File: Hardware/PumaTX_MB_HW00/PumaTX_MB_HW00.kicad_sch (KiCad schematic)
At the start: 107 parts, among them J100 FH12A-26S-0.5SH_55_, J101 FH12-12S-0.5SH_55_, J102 500334-0160, J103 500334-0160, J104 692122030100, J105 53398-0667, J300 U.FL-R-SMT-1_40_, J410 U.FL-R-SMT-1_40_, M130 Motor_DC, M140 Fan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

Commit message: quick esp32 update
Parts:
- U300, U400: footprint Component_lib:ESP32-PICO-D4_1 -> ESP32-PICO-D4_1
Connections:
- net SYS is gone; now on net VSYS: R506.1, R507.1
- net GND: now also U300.49 (GND), U400.49 (GND)
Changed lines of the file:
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@@
     (effects (font (size 1.27 1.27)) (justify right bottom))
   )
-  (label "SYS" (at 449.58 269.24 0)
+  (label "VSYS" (at 449.58 269.24 0)
     (effects (font (size 1.27 1.27)) (justify left bottom))
   )
@@
     (pin "1")
   )
-  (symbol (lib_name "ESP32-PICO-D4_1") (lib_id "Component_lib:ESP32-PICO-D4") (at 73.66 231.14 0) (unit 1)
+  (symbol (lib_id "Component_lib:ESP32-PICO-D4") (at 73.66 231.14 0) (unit 1)
     (in_bom yes) (on_board yes)
     (property "Reference" "U300" (id 0) (at 76.2 223.52 0))
     (property "Value" "ESP32-PICO-D4" (id 1) (at 96.52 248.92 0))
-    (property "Footprint" "Component_lib:ESP32-PICO-D4_1" (id 2) (at 128.27 197.485 0)
+    (property "Footprint" "ESP32-PICO-D4_1" (id 2) (at 128.27 197.485 0)
       (effects (font (size 1.27 1.27)) (justify left) hide)
     )
@@
     (pin "47")
     (pin "48")
+    (pin "49")
     (pin "5")
     (pin "6")
@@
     (pin "2")
   )
-  (symbol (lib_name "ESP32-PICO-D4_1") (lib_id "Component_lib:ESP32-PICO-D4") (at 226.06 231.14 0) (unit 1)
+  (symbol (lib_id "Component_lib:ESP32-PICO-D4") (at 226.06 231.14 0) (unit 1)
     (in_bom yes) (on_board yes)
     (property "Reference" "U400" (id 0) (at 226.06 223.52 0))
     (property "Value" "ESP32-PICO-D4" (id 1) (at 248.92 248.92 0))
-    (property "Footprint" "Component_lib:ESP32-PICO-D4_1" (id 2) (at 280.67 197.485 0)
+    (property "Footprint" "ESP32-PICO-D4_1" (id 2) (at 280.67 197.485 0)
       (effects (font (size 1.27 1.27)) (justify left) hide)
     )
@@
     (pin "47")
     (pin "48")
+    (pin "49")
     (pin "5")
     (pin "6")
@@
     (pin "1")
   )
+  (symbol (lib_id "power:GND") (at 254 248.92 0) (unit 1)
+    (in_bom yes) (on_board yes) (fields_autoplaced)
+    (property "Reference" "#PWR0208" (id 0) (at 254 255.27 0)
+      (effects (font (size 1.27 1.27)) hide)
+    )
+    (property "Value" "GND" (id 1) (at 254 253.3634 0))
+    (property "Footprint" "" (id 2) (at 254 248.92 0)
+      (effects (font (size 1.27 1.27)) hide)
+    )
+    (property "Datasheet" "" (id 3) (at 254 248.92 0)
+      (effects (font (size 1.27 1.27)) hide)
+    )
+    (pin "1")
+  )
   (symbol (lib_id "power:GND") (at 101.6 167.64 0) (mirror y) (unit 1)
     (in_bom yes) (on_board yes) (fields_autoplaced)
@@
     (pin "1")
   )
+  (symbol (lib_id "power:GND") (at 101.6 248.92 0) (unit 1)
+    (in_bom yes) (on_board yes) (fields_autoplaced)
+    (property "Reference" "#PWR0209" (id 0) (at 101.6 255.27 0)
+      (effects (font (size 1.27 1.27)) hide)
+    )
+    (property "Value" "GND" (id 1) (at 101.6 253.3634 0))
+    (property "Footprint" "" (id 2) (at 101.6 248.92 0)
+      (effects (font (size 1.27 1.27)) hide)
+    )
+    (property "Datasheet" "" (id 3) (at 101.6 248.92 0)
+      (effects (font (size 1.27 1.27)) hide)
+    )
+    (pin "1")
+  )
   (symbol (lib_id "Component_lib:R") (at 439.42 246.38 0) (unit 1)
     (in_bom yes) (on_board yes) (fields_autoplaced)
@@
       (reference "#PWR0207") (unit 1) (value "GND") (footprint "")
     )
+    (path "/8a8d2f55-b2eb-4606-93f7-9e68a6db2d19"
+      (reference "#PWR0208") (unit 1) (value "GND") (footprint "")
+    )
+    (path "/a3bb5541-60f1-4243-b6fd-f9f2eee4e164"
+      (reference "#PWR0209") (unit 1) (value "GND") (footprint "")
+    )
     (path "/aa4b37d0-de21-49e4-a60d-a36a4900ab77"
       (reference "#VBAT0101") (unit 1) (value "VBAT") (footprint "")
@@
     )
     (path "/7c01edc0-d7f2-45db-8ab5-251f557b0984"
-      (reference "U300") (unit 1) (value "ESP32-PICO-D4") (footprint "Component_lib:ESP32-PICO-D4_1")
+      (reference "U300") (unit 1) (value "ESP32-PICO-D4") (footprint "ESP32-PICO-D4_1")
     )
     (path "/832e275b-682a-4d6c-91a4-f7dc151a03b6"
-      (reference "U400") (unit 1) (value "ESP32-PICO-D4") (footprint "Component_lib:ESP32-PICO-D4_1")
+      (reference "U400") (unit 1) (value "ESP32-PICO-D4") (footprint "ESP32-PICO-D4_1")
     )
     (path "/6f8f7369-26dc-458b-8b40-9bd8047cb234"

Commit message: working on routing / placement
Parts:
- removed ANT400: 2450AT18A100E, Component_lib:ANTC3216X140N, symbol Component_lib:2450AT18A100E
- removed J300: U.FL-R-SMT-1_40_, Component_lib:u.fl, symbol Component_lib:U.FL-R-SMT-1_40_
- added ANT300: 2450AT18A100E, Component_lib:ANTC3216X140N, symbol Component_lib:2450AT18A100E
- added C130, C140: 100n, Capacitor_SMD:C_0402_1005Metric, symbol Component lib:C
- added J400: U.FL-R-SMT-1_40_, Component_lib:u.fl, symbol Component_lib:U.FL-R-SMT-1_40_
- added R305: 120k, Capacitor_SMD:C_0402_1005Metric, symbol Component lib:R
- added R306: 470k, Capacitor_SMD:C_0402_1005Metric, symbol Component lib:R
- added R511, R512: 0, Capacitor_SMD:C_0201_0603Metric, symbol Component lib:R
- added TP105: BAT_WHITE, TestPoint:TestPoint_Pad_D1.0mm, symbol Connector:TestPoint
- added TP302: CRSF, TestPoint:TestPoint_Pad_D1.0mm, symbol Connector:TestPoint
- TP300, TP301, TP401: footprint TestPoint:TestPoint_Pad_D1.5mm -> TestPoint:TestPoint_Pad_D1.0mm
- TP400: value TestPoint -> ELRS_CHIP_PU; footprint TestPoint:TestPoint_Pad_D1.5mm -> TestPoint:TestPoint_Pad_D1.0mm
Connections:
- net LED_ANODE is gone; now on net LED: J100.10
- net LED_CATHODE is gone; now on net GND: J100.14
- net 50_ESP_ELRS_ANT_2: now also J400.1 (ant)
- net 50_PUMATX_ANT_2: now also ANT300.1 (A)
- net BATTERY_VOLTAGE: now also R305.2, R306.1
- net BATTERY_WHITE: now also TP105.1
- net CRSF: now also TP302.1
- net DISPLAY_BACKLIGHT: now also R511.1
- net FAN_LS: now also C140.1
- net GND: now also U410.25 (GND), J400.2 (gnd), J400.3 (gnd), R306.2
- net HAPTIC_LS: now also C130.1
- net LED: now also R512.1; no longer U520.4 (EN), U530.4 (EN)
- net VBAT: now also R305.1
- net VSYS: now also C130.2, C140.2
- new net AUX_EN: R511.2, R512.2, U520.4 (EN), U530.4 (EN)
- no-connect marks 43 -> 44
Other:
- moved on the sheet: D130, D140, M130, M140

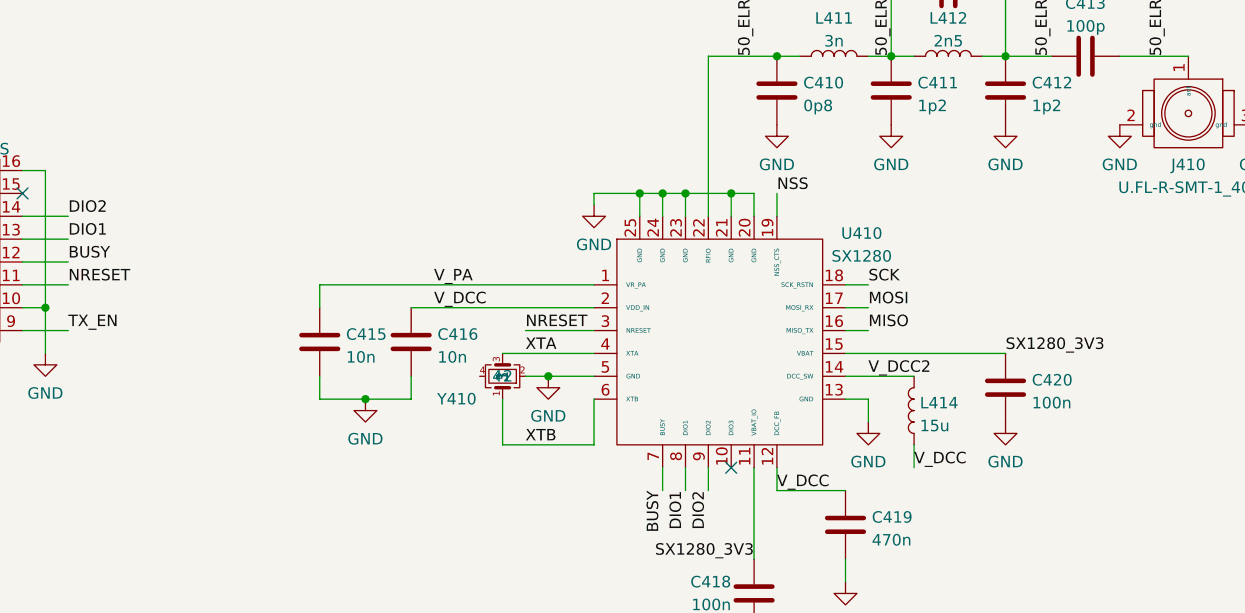
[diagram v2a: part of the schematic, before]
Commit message: Done SX1280 routing and half of RF
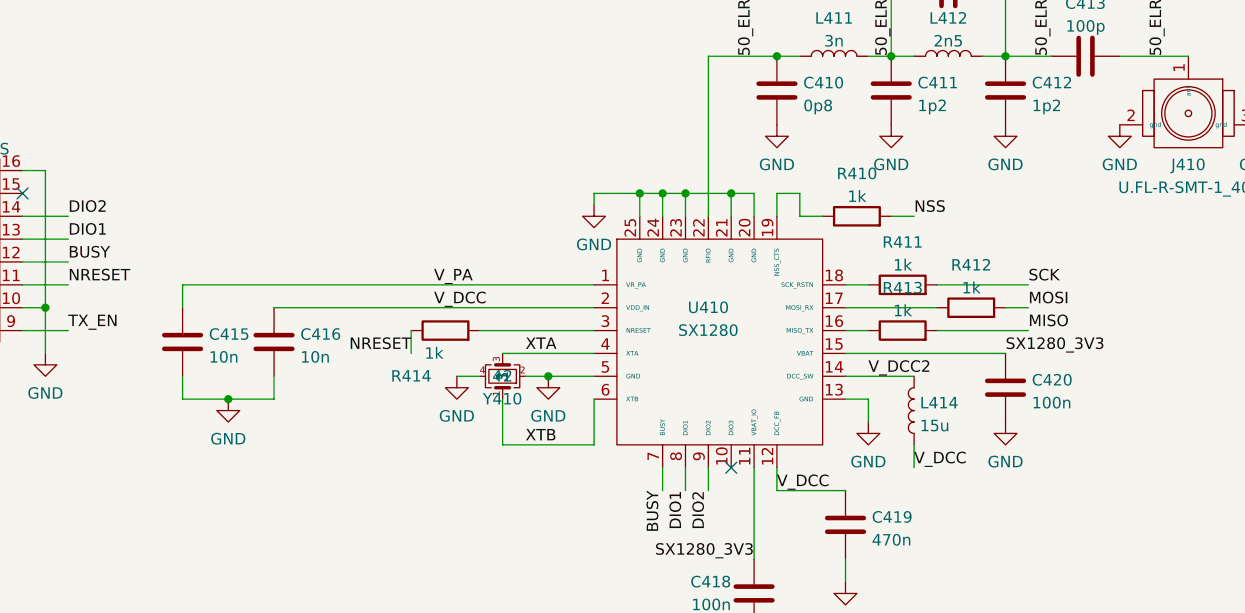
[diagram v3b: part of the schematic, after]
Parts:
- added R410, R411, R412, R413, R414: 1k, Capacitor_SMD:C_0201_0603Metric, symbol Component_lib:R
- C110, C120, C201, C203, C350, C418, C420, C450: footprint Capacitor_SMD:C_0603_1608Metric -> Capacitor_SMD:C_0402_1005Metric
- C306, C307, C406, C407: footprint Capacitor_SMD:C_0402_1005Metric -> Capacitor_SMD:C_0201_0603Metric
- C410, C411, C412, C413, C414: footprint Capacitor_SMD:C_0603_1608Metric -> Capacitor_SMD:C_0201_0603Metric
- U300, U400: footprint ESP32-PICO-D4_1 -> Component_lib:ESP32-PICO-D4_1
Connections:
- net GND: now also Y410.4
- net MISO: now also R413.2; no longer U410.16 (MISO_TX)
- net MOSI: now also R412.2; no longer U410.17 (MOSI_RX)
- net NRESET: now also R414.1; no longer U410.3 (NRESET)
- net NSS: now also R410.2; no longer U410.19 (NSS_CTS)
- net SCK: now also R411.2; no longer U410.18 (SCK_RSTN)
- new net: R413.1, U410.16 (MISO_TX)
- new net: R412.1, U410.17 (MOSI_RX)
- new net: R411.1, U410.18 (SCK_RSTN)
- new net: R410.1, U410.19 (NSS_CTS)
- new net: R414.2, U410.3 (NRESET)
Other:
- moved on the sheet: C415, C416

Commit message: and on and on and on... It is getting harder
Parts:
- C201: footprint Capacitor_SMD:C_0402_1005Metric -> Capacitor_SMD:C_0603_1608Metric
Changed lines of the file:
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@@
       (effects (font (size 1.27 1.27)) (justify left))
     )
-    (property "Footprint" "Capacitor_SMD:C_0402_1005Metric" (id 2) (at 376.8852 88.9 0)
+    (property "Footprint" "Capacitor_SMD:C_0603_1608Metric" (id 2) (at 376.8852 88.9 0)
       (effects (font (size 1.27 1.27)) hide)
     )
@@
     )
     (path "/992d47c1-3d77-49c3-9a69-0e410ebfa256"
-      (reference "C201") (unit 1) (value "100n") (footprint "Capacitor_SMD:C_0402_1005Metric")
+      (reference "C201") (unit 1) (value "100n") (footprint "Capacitor_SMD:C_0603_1608Metric")
     )
     (path "/ece295b9-b570-401a-92a8-013600552bb1"

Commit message: Wow its gonna be complicated
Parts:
- added R101, R102: 0k, Capacitor_SMD:C_0402_1005Metric, symbol Component_lib:R
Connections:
- net RX_PUMATX_DEBUG: now also R102.2; no longer J104.6 (SSRX+)
- net TX_PUMATX_DEBUG: now also R101.2; no longer J104.5 (SSRX-)
- net VBUS: now also J104.2 (D-); no longer J104.1 (VBUS)
- net VSYS: now also J104.1 (VBUS); no longer J104.2 (D-)
- new net: J104.5 (SSRX-), R101.1
- new net: J104.6 (SSRX+), R102.1
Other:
- moved on the sheet: J104

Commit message: Almost done !! only 3 PSU to go
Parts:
- R300, R301, R302, R303, R304, R401: footprint Capacitor_SMD:C_0402_1005Metric -> Capacitor_SMD:C_0201_0603Metric
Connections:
- net C1: now also U300.36 (GPIO23); no longer U300.39 (GPIO22)
- net C2: now also U300.11 (GPIO35); no longer U300.38 (GPIO19)
- net LEFT: now also U300.38 (GPIO19); no longer U300.6 (SENSOR_CAPP/GPIO37)
- net LEFT_POT: now also U300.5 (SENSOR_VP/GPIO36); no longer U300.11 (GPIO35)
- net OK: now also U300.35 (GPIO18); no longer U300.25 (GPIO16)
- net PAUSE: now also U300.21 (MTDO/GPIO15); no longer U300.34 (GPIO5)
- net PHOTO: now also U300.6 (SENSOR_CAPP/GPIO37); no longer U300.36 (GPIO23)
- net PUMATX_SCL: now also U300.15 (GPIO26); no longer U300.14 (GPIO25)
- net PUMATX_SDA: now also U300.14 (GPIO25); no longer U300.15 (GPIO26)
- net RECORD: now also U300.7 (SENSOR_CAPN/GPIO38); no longer U300.21 (MTDO/GPIO15)
- net RIGHT: now also U300.39 (GPIO22); no longer U300.5 (SENSOR_VP/GPIO36)
- net RTH: now also U300.25 (GPIO16); no longer U300.35 (GPIO18)
- net UP: now also U300.34 (GPIO5); no longer U300.7 (SENSOR_CAPN/GPIO38)
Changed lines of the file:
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@@
     (effects (font (size 1.27 1.27)) (justify left bottom))
   )
-  (label "LEFT_POT" (at 71.12 256.54 180)
+  (label "LEFT_POT" (at 71.12 241.3 180)
     (effects (font (size 1.27 1.27)) (justify right bottom))
   )
@@
     (effects (font (size 1.27 1.27)) (justify left bottom))
   )
-  (label "PUMATX_SDA" (at 86.36 269.24 270)
+  (label "PUMATX_SDA" (at 83.82 269.24 270)
     (effects (font (size 1.27 1.27)) (justify right bottom))
   )
-  (label "UP" (at 71.12 246.38 180)
-    (effects (font (size 1.27 1.27)) (justify right bottom))
+  (label "UP" (at 119.38 236.22 0)
+    (effects (font (size 1.27 1.27)) (justify left bottom))
   )
   (label "PUMATX_CHIP_PU" (at 38.1 365.76 180)
@@
     (effects (font (size 1.27 1.27)) (justify left bottom))
   )
-  (label "RIGHT" (at 71.12 241.3 180)
-    (effects (font (size 1.27 1.27)) (justify right bottom))
+  (label "RIGHT" (at 104.14 220.98 90)
+    (effects (font (size 1.27 1.27)) (justify left bottom))
   )
   (label "SX1280_3V3" (at 307.34 388.62 180)
@@
     (effects (font (size 1.27 1.27)) (justify right bottom))
   )
-  (label "C2" (at 106.68 220.98 90)
-    (effects (font (size 1.27 1.27)) (justify left bottom))
+  (label "C2" (at 71.12 256.54 180)
+    (effects (font (size 1.27 1.27)) (justify right bottom))
   )
   (label "MISO" (at 259.08 220.98 90)
@@
     (effects (font (size 1.27 1.27)) (justify right bottom))
   )
-  (label "C1" (at 104.14 220.98 90)
+  (label "C1" (at 119.38 231.14 0)
     (effects (font (size 1.27 1.27)) (justify left bottom))
   )
@@
     (effects (font (size 1.27 1.27)) (justify left bottom))
   )
-  (label "RECORD" (at 101.6 269.24 270)
+  (label "RECORD" (at 71.12 246.38 180)
     (effects (font (size 1.27 1.27)) (justify right bottom))
   )
@@
     (effects (font (size 1.27 1.27)) (justify left bottom))
   )
-  (label "PHOTO" (at 119.38 231.14 0)
-    (effects (font (size 1.27 1.27)) (justify left bottom))
+  (label "PHOTO" (at 71.12 243.84 180)
+    (effects (font (size 1.27 1.27)) (justify right bottom))
   )
   (label "BQ_CHG" (at 454.66 289.56 180)
     (effects (font (size 1.27 1.27)) (justify right bottom))
   )
-  (label "RTH" (at 119.38 233.68 0)
+  (label "RTH" (at 119.38 259.08 0)
     (effects (font (size 1.27 1.27)) (justify left bottom))
   )
@@
     (effects (font (size 1.27 1.27)) (justify right bottom))
   )
-  (label "PUMATX_SCL" (at 83.82 269.24 270)
+  (label "PUMATX_SCL" (at 86.36 269.24 270)
     (effects (font (size 1.27 1.27)) (justify right bottom))
   )
@@
     (effects (font (size 1.27 1.27)) (justify left bottom))
   )
-  (label "LEFT" (at 71.12 243.84 180)
-    (effects (font (size 1.27 1.27)) (justify right bottom))
+  (label "LEFT" (at 106.68 220.98 90)
+    (effects (font (size 1.27 1.27)) (justify left bottom))
   )
   (label "RX_EN" (at 241.3 269.24 270)
@@
     (effects (font (size 1.27 1.27)) (justify left bottom))
   )
-  (label "PAUSE" (at 119.38 236.22 0)
-    (effects (font (size 1.27 1.27)) (justify left bottom))
+  (label "PAUSE" (at 101.6 269.24 270)
+    (effects (font (size 1.27 1.27)) (justify right bottom))
   )
   (label "RIGHT_POT" (at 71.12 259.08 180)
@@
     (effects (font (size 1.27 1.27)) (justify right bottom))
   )
-  (label "OK" (at 119.38 259.08 0)
+  (label "OK" (at 119.38 233.68 0)
     (effects (font (size 1.27 1.27)) (justify left bottom))
   )
@@
       (effects (font (size 1.27 1.27)) (justify left))
     )
-    (property "Footprint" "Capacitor_SMD:C_0402_1005Metric" (id 2) (at 214.122 303.53 90)
+    (property "Footprint" "Capacitor_SMD:C_0201_0603Metric" (id 2) (at 214.122 303.53 90)
       (effects (font (size 1.27 1.27)) hide)
     )
@@
       (effects (font (size 1.27 1.27)) (justify left))
     )
-    (property "Footprint" "Capacitor_SMD:C_0402_1005Metric" (id 2) (at 38.862 359.41 90)
+    (property "Footprint" "Capacitor_SMD:C_0201_0603Metric" (id 2) (at 38.862 359.41 90)
       (effects (font (size 1.27 1.27)) hide)
     )
@@
       (effects (font (size 1.27 1.27)) (justify left))
     )
-    (property "Footprint" "Capacitor_SMD:C_0402_1005Metric" (id 2) (at 79.502 311.15 90)
+    (property "Footprint" "Capacitor_SMD:C_0201_0603Metric" (id 2) (at 79.502 311.15 90)
       (effects (font (size 1.27 1.27)) hide)
     )
@@
       (effects (font (size 1.27 1.27)) (justify left))
     )
-    (property "Footprint" "Capacitor_SMD:C_0402_1005Metric" (id 2) (at 49.022 311.15 90)
+    (property "Footprint" "Capacitor_SMD:C_0201_0603Metric" (id 2) (at 49.022 311.15 90)
       (effects (font (size 1.27 1.27)) hide)
     )
@@
       (effects (font (size 1.27 1.27)) (justify left))
     )
-    (property "Footprint" "Capacitor_SMD:C_0402_1005Metric" (id 2) (at 64.262 311.15 90)
+    (property "Footprint" "Capacitor_SMD:C_0201_0603Metric" (id 2) (at 64.262 311.15 90)
       (effects (font (size 1.27 1.27)) hide)
     )
@@
       (effects (font (size 1.27 1.27)) (justify left))
     )
-    (property "Footprint" "Capacitor_SMD:C_0402_1005Metric" (id 2) (at 33.782 311.15 90)
+    (property "Footprint" "Capacitor_SMD:C_0201_0603Metric" (id 2) (at 33.782 311.15 90)
       (effects (font (size 1.27 1.27)) hide)
     )
@@
     )
     (path "/3b6bde78-5a55-4be5-bdd1-600e9f0e059a"
-      (reference "R300") (unit 1) (value "10k") (footprint "Capacitor_SMD:C_0402_1005Metric")
+      (reference "R300") (unit 1) (value "10k") (footprint "Capacitor_SMD:C_0201_0603Metric")
     )
     (path "/dd1cb709-1edc-4c69-b59e-177f0a25213d"
-      (reference "R301") (unit 1) (value "2k2") (footprint "Capacitor_SMD:C_0402_1005Metric")
+      (reference "R301") (unit 1) (value "2k2") (footprint "Capacitor_SMD:C_0201_0603Metric")
     )
     (path "/afa4d3b8-c1d7-46a3-a296-9ce19b79d602"
-      (reference "R302") (unit 1) (value "2k2") (footprint "Capacitor_SMD:C_0402_1005Metric")
+      (reference "R302") (unit 1) (value "2k2") (footprint "Capacitor_SMD:C_0201_0603Metric")
     )
     (path "/d29f1db4-a8a4-4188-8fc6-6dc699ab160b"
-      (reference "R303") (unit 1) (value "2k2") (footprint "Capacitor_SMD:C_0402_1005Metric")
+      (reference "R303") (unit 1) (value "2k2") (footprint "Capacitor_SMD:C_0201_0603Metric")
     )
     (path "/5e8ac63c-6e55-48d6-b4f9-098f6f8bc775"
-      (reference "R304") (unit 1) (value "2k2") (footprint "Capacitor_SMD:C_0402_1005Metric")
+      (reference "R304") (unit 1) (value "2k2") (footprint "Capacitor_SMD:C_0201_0603Metric")
     )
     (path "/0f6ac3cc-6193-4788-bc92-b77039d5ad01"
@@
     )
     (path "/33c7f00b-df21-4afa-814f-7fee256513fa"
-      (reference "R401") (unit 1) (value "10k") (footprint "Capacitor_SMD:C_0402_1005Metric")
+      (reference "R401") (unit 1) (value "10k") (footprint "Capacitor_SMD:C_0201_0603Metric")
     )
     (path "/3f57d1b7-0d24-41e1-a455-e642864df774"
